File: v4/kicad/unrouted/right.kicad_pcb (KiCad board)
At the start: 2 copper layers, 160 x 118.6 mm, 72 parts

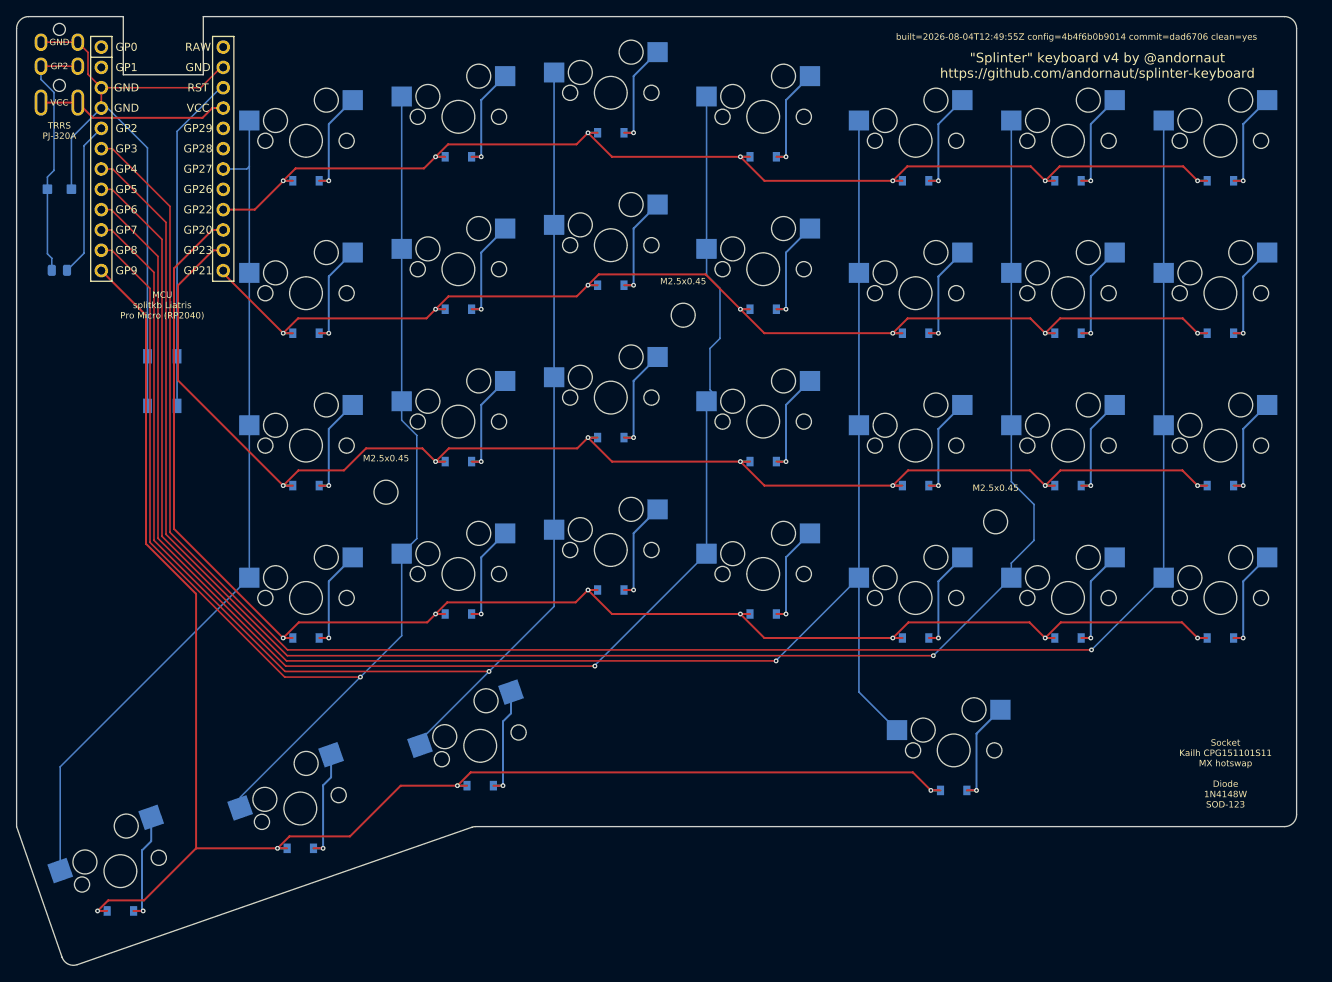
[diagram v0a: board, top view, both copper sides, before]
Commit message: Mirror the halves by construction, and gate that they stay mirrored
The halves' outer board edges were anchored to their own pinky columns, which
differ (left 1.5u; right 1u plus the extra inner column). The left edge picked
up a 0.25mm tilt, so the two outlines were never mirror images and every
clearance measured from that edge differed between the halves. Nothing saw it:
both boards route, pass DRC, fab and assemble.

Both edges now come from one mirrored pair of anchors, edge_outer_top and
edge_outer_bottom, whose base points sit on the right half because that is
where the edge is constrained by a 0.5mm keycap gap. The left half's pinky has
about 10mm of margin and follows the mirror. Only the left bottom corner moves,
0.25mm outward, so every clearance there grows.

validate:symmetry (pipeline step 6) holds the halves to it: the Edge.Cuts
outlines by Hausdorff distance, then every footprint, pad, rule area and silk
text. Pads are matched by name as well as position, since a two-pin part
rotated 180 leaves its pad positions unchanged and swaps which net sits at
each; that is what pins the TVS's compensating rotation in place. Switches,
matrix diodes and the MCU are held to mirrored placement and orientation
instead, because their pin fields are physically not mirror-symmetric. Hand
routing is not compared.

The board halves are regenerated from the new config.
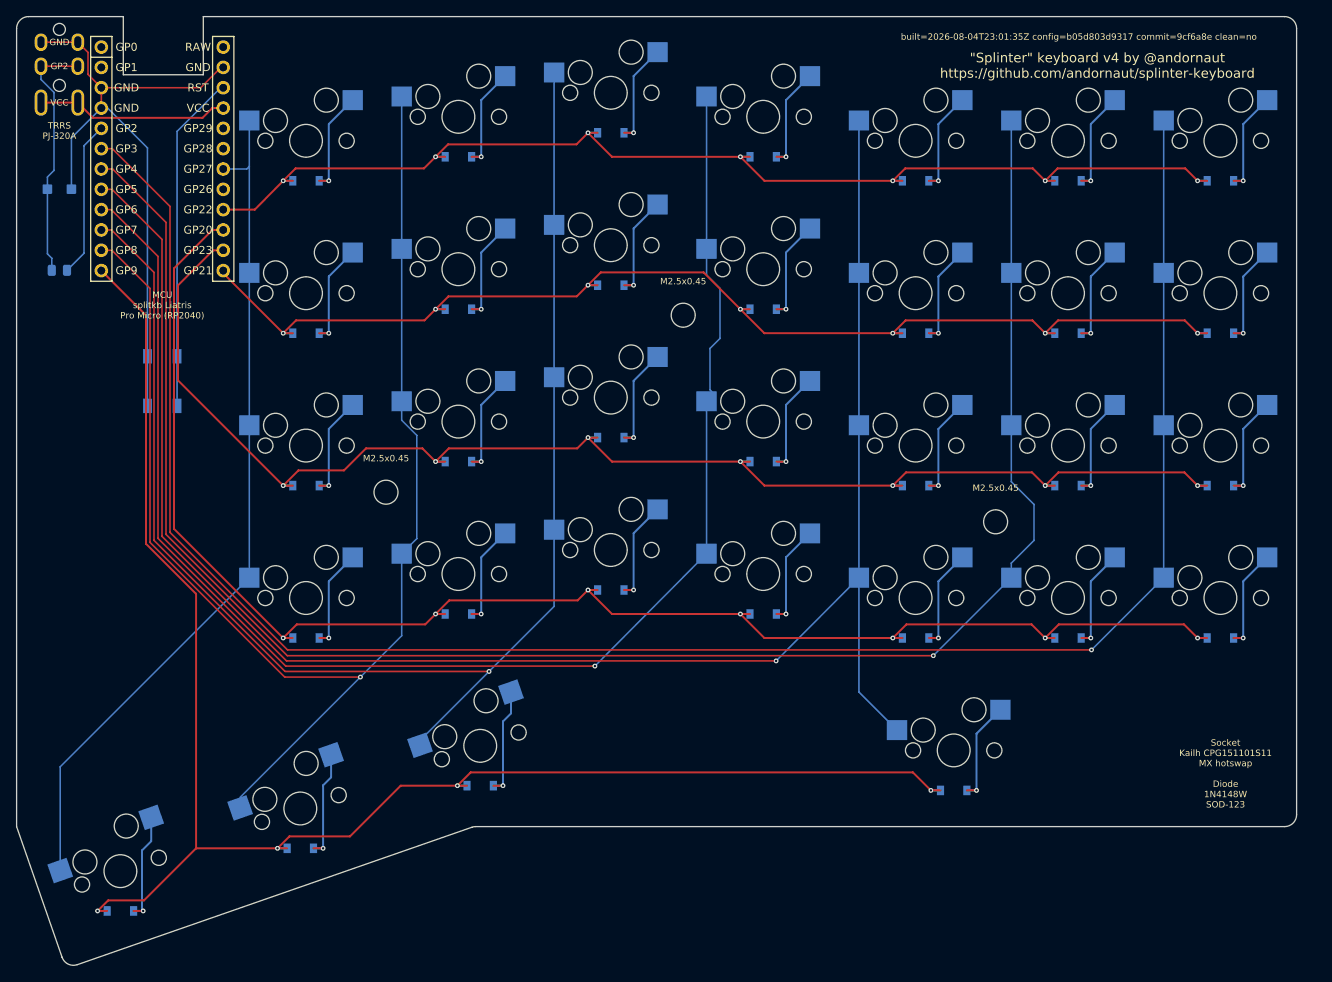
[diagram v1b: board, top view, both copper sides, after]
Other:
- board text added: "built=2026-08-04T23:01:35Z config=b05d803d9317 commit=9cf6a8e clean=no"
- board text removed: "built=2026-08-04T12:49:55Z config=4b4f6b0b9014 commit=dad6706 clean=yes"

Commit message: New release version
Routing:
- net P10: track 150.6 -> 142.5 mm
- net P14: track 198.9 -> 190.9 mm
- net P16: track 178.1 -> 170.1 mm
- net P15: track 147.6 -> 139.7 mm
- net P9: track 199.0 -> 194.2 mm
- net dash_upper: track 13.7 -> 12.5 mm, vias 1 -> 0
- net dash_num: track 13.7 -> 12.5 mm, vias 1 -> 0
- net dash_lower: track 13.7 -> 12.5 mm, vias 1 -> 0
- net dash_home: track 13.7 -> 12.5 mm, vias 1 -> 0
- net zero_upper: track 13.7 -> 12.5 mm, vias 1 -> 0
- net zero_num: track 13.7 -> 12.5 mm, vias 1 -> 0
- net zero_lower: track 13.7 -> 12.5 mm, vias 1 -> 0
- net zero_home: track 13.7 -> 12.5 mm, vias 1 -> 0
- net mirror_three_mod: track 14.5 -> 13.3 mm, vias 1 -> 0
- net mirror_four_upper: track 13.7 -> 12.5 mm, vias 1 -> 0
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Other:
- board text added: "built=2026-08-04T12:49:55Z config=4b4f6b0b9014 commit=dad6706 clean=yes"
- board text removed: "built=2026-08-04T23:01:35Z config=b05d803d9317 commit=9cf6a8e clean=no"

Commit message: New release version
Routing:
- net mirror_five_mod: track 14.4 -> 13.4 mm
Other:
- board text added: "built=2026-08-04T23:55:37Z config=b05d803d9317 commit=96388f1 clean=no"
- board text removed: "built=2026-08-04T12:49:55Z config=4b4f6b0b9014 commit=dad6706 clean=yes"

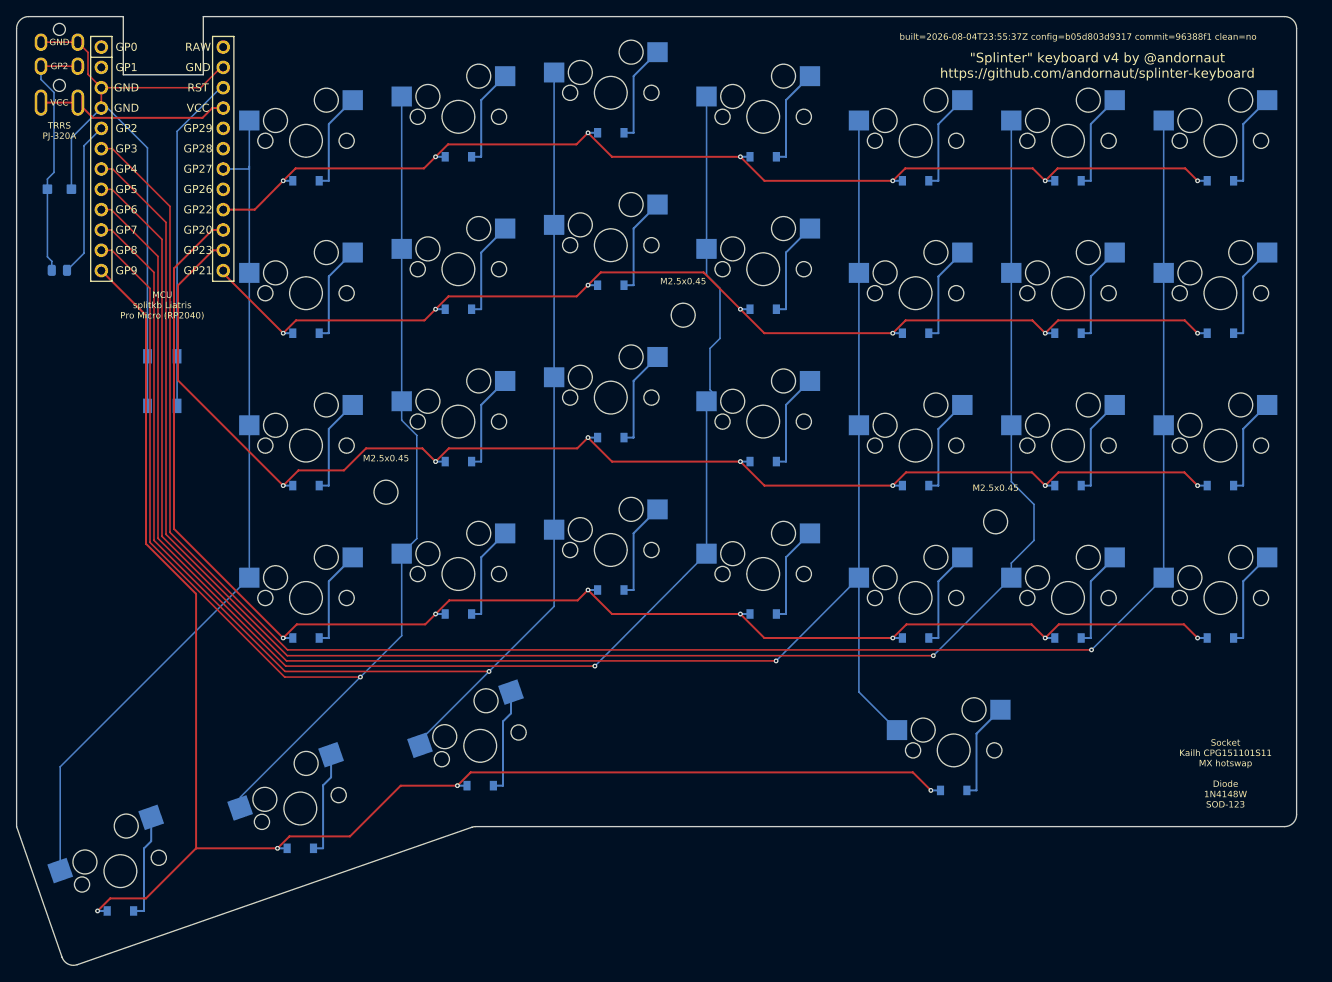
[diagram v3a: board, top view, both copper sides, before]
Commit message: Delete copper buried inside a track of its own net, and say how to rebuild
cleanup-tracks.py keyed duplicates on an exact path, so a segment lying along a
longer one of the same net shared no key with it and outlived every rule here:
both ends sit on the cover's copper, so it is not dangling, and it is not in a
pad. Doubled copper carrying its own net is invisible to DRC, so it reached the
master unremarked. Add a containment rule: same layer, both ends on the other's
centreline, no wider than it, which together mean the copper is already there,
so the delete moves nothing and strands nothing.

Also state each half's dimensions pre- and post-fillet as tables, split the
case-modelling guidance into the rules it was already a list of, and record that
reproducing a build means checking its commit out and re-running the pipeline.
Lifting kicad/routed/ from that commit gives the previous build's masters, since
a stamp can only ever name its own parent.
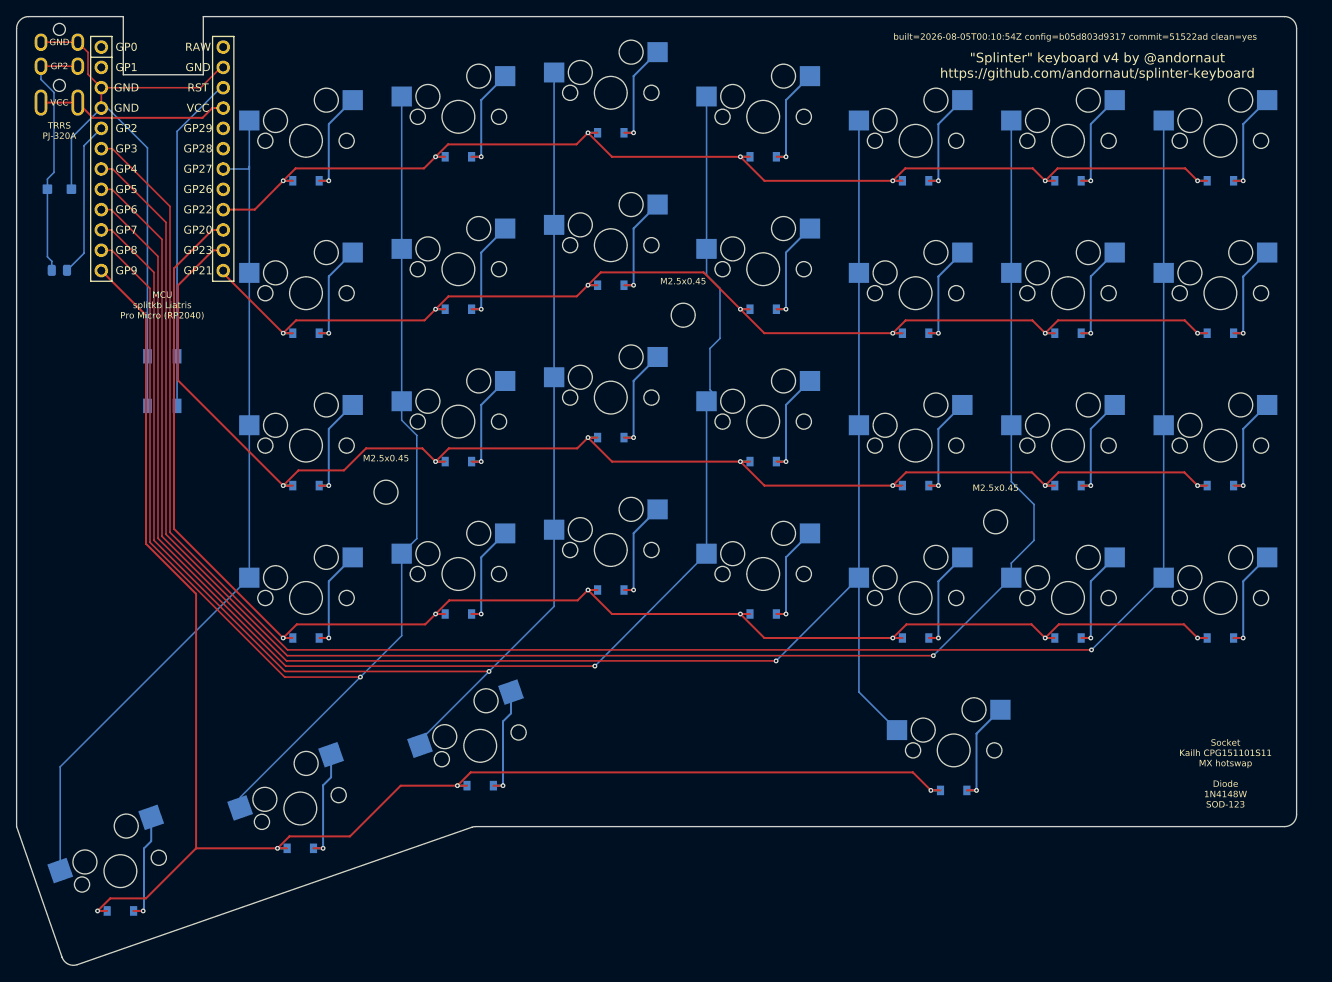
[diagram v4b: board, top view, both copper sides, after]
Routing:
- net P16: track 169.7 -> 178.1 mm
- net P14: track 190.5 -> 198.9 mm
- net P10: track 142.2 -> 150.6 mm
- net P15: track 139.2 -> 147.6 mm
- net P9: track 194.2 -> 199.0 mm
- net mirror_five_mod: track 13.4 -> 15.8 mm, vias 0 -> 1
- net dash_upper: track 12.5 -> 13.7 mm, vias 0 -> 1
- net dash_num: track 12.5 -> 13.7 mm, vias 0 -> 1
- net dash_lower: track 12.5 -> 13.7 mm, vias 0 -> 1
- net dash_home: track 12.5 -> 13.7 mm, vias 0 -> 1
- net zero_upper: track 12.5 -> 13.7 mm, vias 0 -> 1
- net zero_num: track 12.5 -> 13.7 mm, vias 0 -> 1
- net zero_lower: track 12.5 -> 13.7 mm, vias 0 -> 1
- net zero_home: track 12.5 -> 13.7 mm, vias 0 -> 1
- net mirror_three_mod: track 13.3 -> 14.5 mm, vias 0 -> 1
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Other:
- board text added: "built=2026-08-05T00:10:54Z config=b05d803d9317 commit=51522ad clean=yes"
- board text removed: "built=2026-08-04T23:55:37Z config=b05d803d9317 commit=96388f1 clean=no"

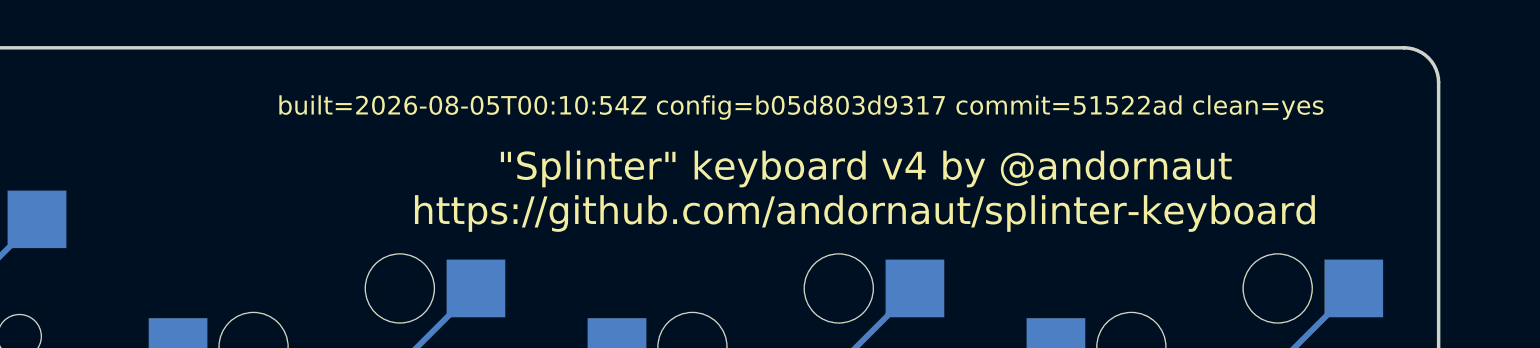
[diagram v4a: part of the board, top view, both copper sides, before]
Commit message: Rebuild the boards with the buried-copper rule in force
The right master loses the include_traces_vias stub a route had run along, plus
the collinear fragments the delete freed for the merge: 337 segments to 334. The
left half was already clean. Every gate passes.
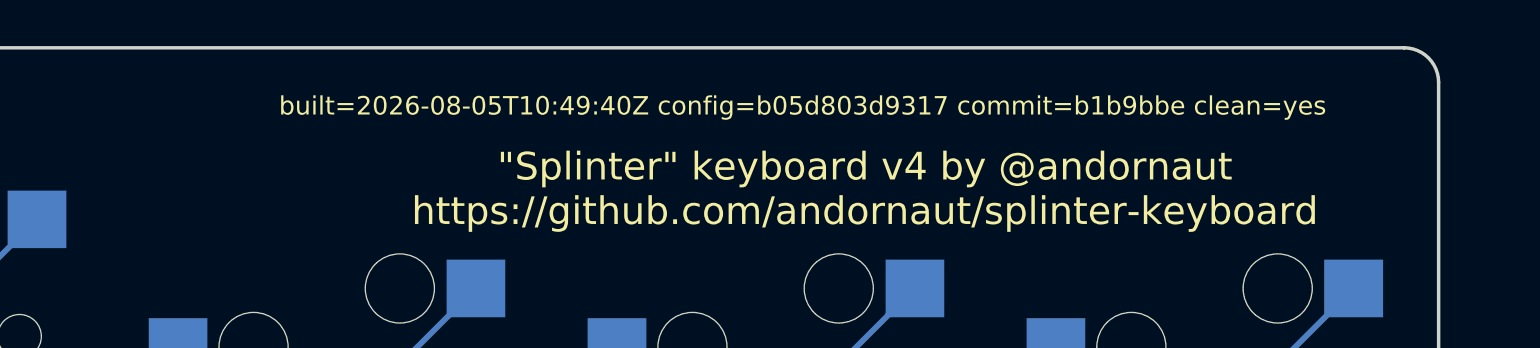
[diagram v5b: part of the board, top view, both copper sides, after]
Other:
- board text added: "built=2026-08-05T10:49:40Z config=b05d803d9317 commit=b1b9bbe clean=yes"
- board text removed: "built=2026-08-05T00:10:54Z config=b05d803d9317 commit=51522ad clean=yes"

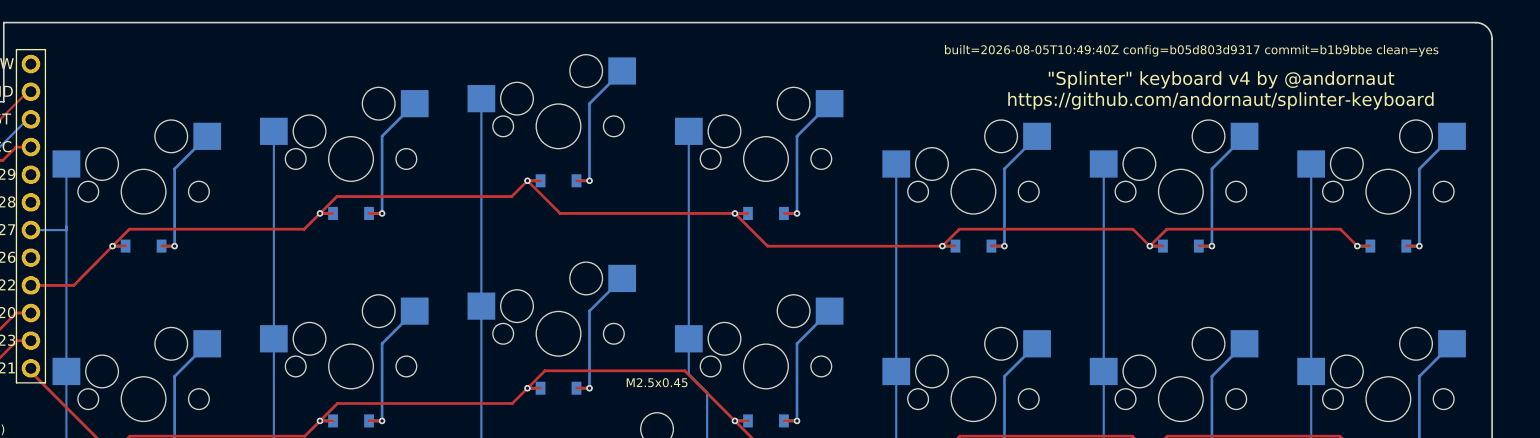
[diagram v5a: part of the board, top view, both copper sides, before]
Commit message: Rebuild the boards on the relocated scripts
Copper, pads, zones and outline are identical to the previous build; the boards
differ only in their provenance stamp and regenerated UUIDs. Every gate passes.
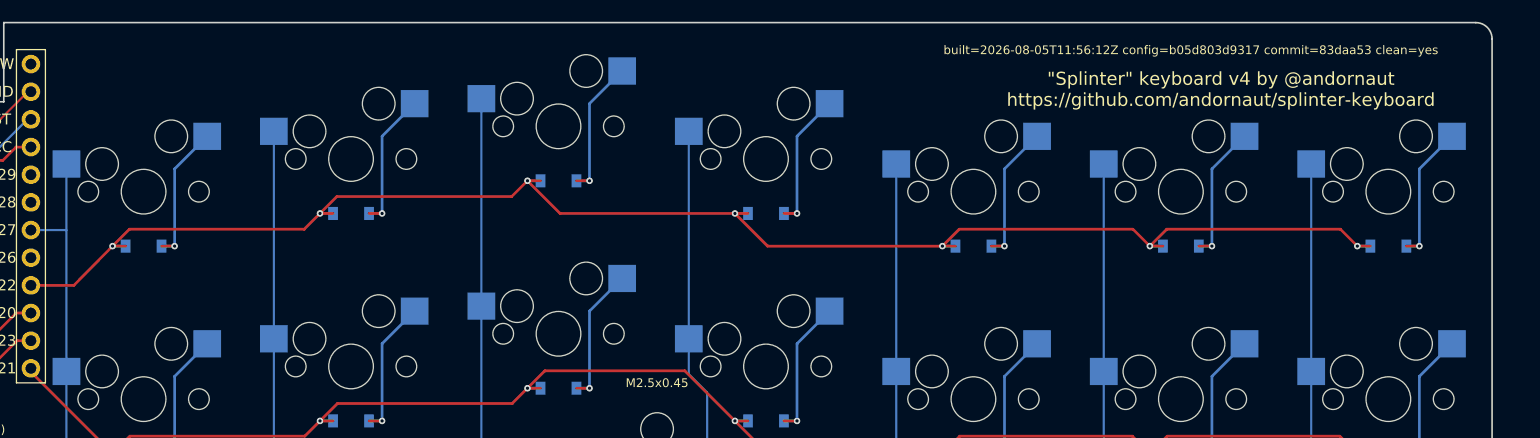
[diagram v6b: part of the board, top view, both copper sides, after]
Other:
- board text added: "built=2026-08-05T11:56:12Z config=b05d803d9317 commit=83daa53 clean=yes"
- board text removed: "built=2026-08-05T10:49:40Z config=b05d803d9317 commit=b1b9bbe clean=yes"
